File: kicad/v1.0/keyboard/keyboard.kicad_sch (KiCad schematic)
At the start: 89 parts, among them J1 PMOD, J2 Conn_01x02, J3 Conn_01x02, SW1 @, SW10 I, SW11 J, SW12 K, SW13 L, SW14 M, SW15 N, SW16 O, SW17 P, SW18 Q, SW19 R, SW2 A, SW20 S, SW21 T, SW22 U, SW23 V, SW24 W, SW25 X, SW26 Y, SW27 Z, SW28 0, SW29 1, SW3 B, SW30 2, SW31 3, SW32 4, SW33 5, SW34 6, SW35 7, SW36 0, SW37 1, SW38 2, SW39 3, SW4 C, SW40 4, SW41 5, SW42 6, SW43 7, SW44 8, SW45 9, SW46 ., SW47 8, SW48 9, SW49 :, SW5 D, SW50 ;, SW51 ,, SW52 -, SW53 ., SW54 /, SW55 ENTER, SW56 ENTER, SW57 CLEAR, SW58 BREAK, SW59 UP, SW6 E, SW60 DOWN, SW61 LEFT, SW62 RIGHT, SW63 SPACE, SW64 RESET, SW65 RSHIFT, SW66 LSHIFT, SW67 SPACE, SW68 SPACE, SW69 ENTER, SW7 F, SW8 G, SW9 H, U1 74LS07, U2 74LS138, U3 74LS07, U4 74LS157

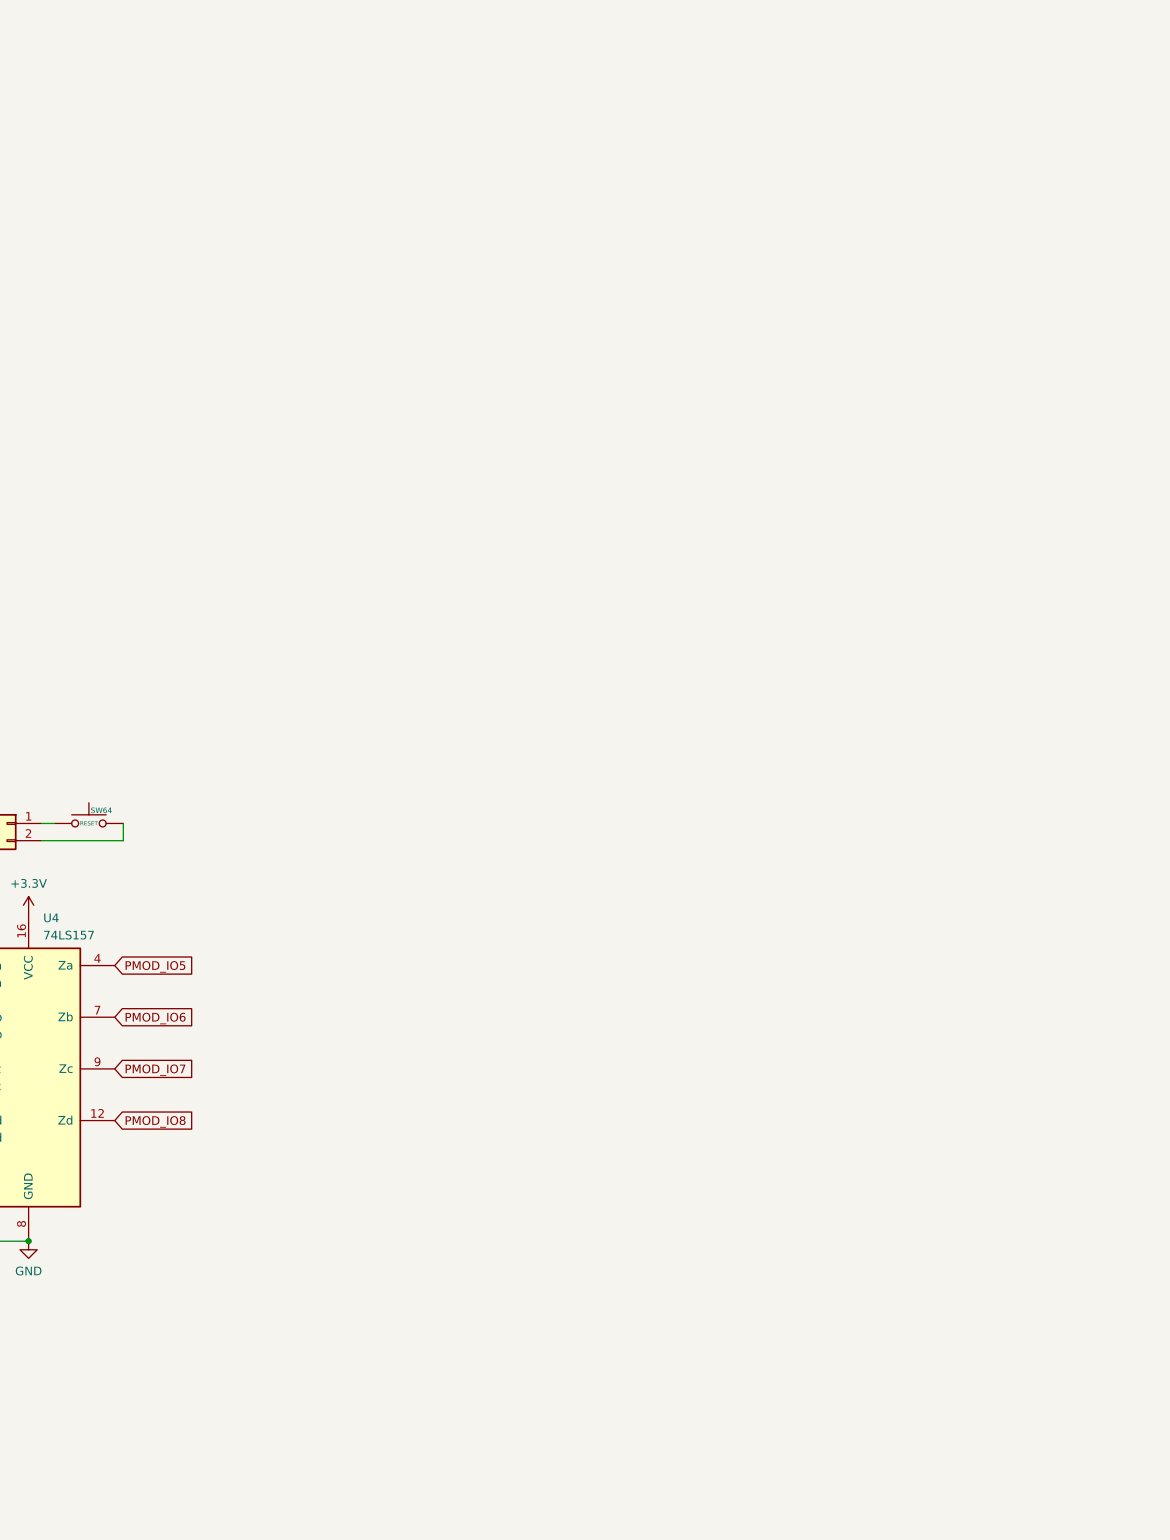
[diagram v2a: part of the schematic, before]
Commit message: Add schematics for interface PCB
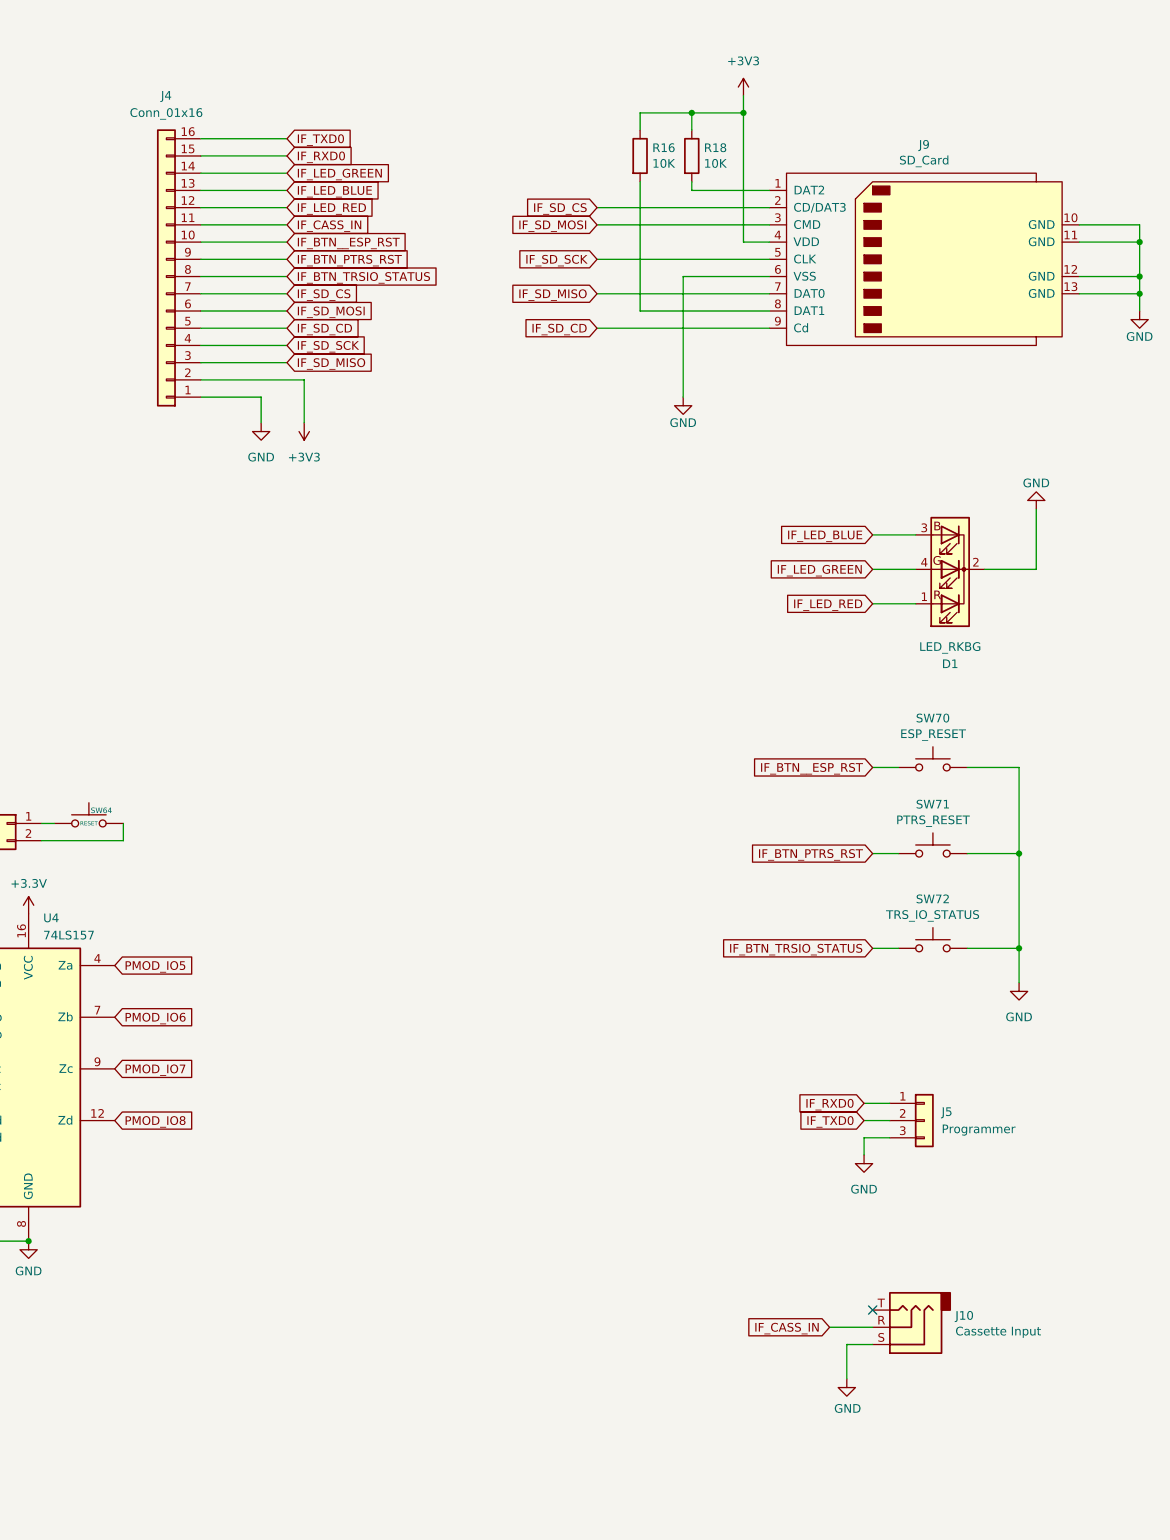
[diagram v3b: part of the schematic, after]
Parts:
- added D1: LED_RKBG, LED_THT:LED_D5.0mm-4_RGB, symbol Device:LED_RKBG
- added J10: Cassette Input, Library:Jack_3.5mm_CUI_SJ1-3535NG_Horizontal_CircularHoles, symbol Connector:AudioJack3
- added J4: Conn_01x16, Connector_PinHeader_2.54mm:PinHeader_1x16_P2.54mm_Vertical, symbol Connector_Generic:Conn_01x16
- added J5: Programmer, Connector_PinHeader_2.54mm:PinHeader_1x03_P2.54mm_Horizontal, symbol Connector_Generic:Conn_01x03
- added J9: SD_Card, Library:TFP09-2-12B, symbol SDCard:SD_Card
- added R16, R18: 10K, Resistor_SMD:R_0805_2012Metric_Pad1.20x1.40mm_HandSolder, symbol Device:R
- added SW70: ESP_RESET, Button_Switch_THT:SW_PUSH_6mm, symbol Switch:SW_Push
- added SW71: PTRS_RESET, Button_Switch_THT:SW_PUSH_6mm, symbol Switch:SW_Push
- added SW72: TRS_IO_STATUS, Button_Switch_THT:SW_PUSH_6mm, symbol Switch:SW_Push
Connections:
- net GND: now also D1.2 (K), J10.S, J4.1 (Pin_1), J5.3 (Pin_3), J9.10 (GND), J9.11 (GND), J9.12 (GND), J9.13 (GND), J9.6 (VSS), SW70.2, SW71.2, SW72.2
- new net: J9.1 (DAT2), R18.2
- new net: J9.8 (DAT1), R16.2
- new net +3V3: J4.2 (Pin_2), J9.4 (VDD), R16.1, R18.1
- new net IF_BTN_PTRS_RST: J4.9 (Pin_9), SW71.1
- new net IF_BTN_TRSIO_STATUS: J4.8 (Pin_8), SW72.1
- new net IF_BTN__ESP_RST: J4.10 (Pin_10), SW70.1
- new net IF_CASS_IN: J10.R, J4.11 (Pin_11)
- new net IF_LED_BLUE: D1.3 (BA), J4.13 (Pin_13)
- new net IF_LED_GREEN: D1.4 (GA), J4.14 (Pin_14)
- new net IF_LED_RED: D1.1 (RA), J4.12 (Pin_12)
- new net IF_RXD0: J4.15 (Pin_15), J5.1 (Pin_1)
- new net IF_SD_CD: J4.5 (Pin_5), J9.9 (Cd)
- new net IF_SD_CS: J4.7 (Pin_7), J9.2 (CD/DAT3)
- new net IF_SD_MISO: J4.3 (Pin_3), J9.7 (DAT0)
- new net IF_SD_MOSI: J4.6 (Pin_6), J9.3 (CMD)
- new net IF_SD_SCK: J4.4 (Pin_4), J9.5 (CLK)
- new net IF_TXD0: J4.16 (Pin_16), J5.2 (Pin_2)
- no-connect marks 4 -> 5

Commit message: Updated Interface board
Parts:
- removed J10: Cassette Input, Library:Jack_3.5mm_CUI_SJ1-3535NG_Horizontal_CircularHoles, symbol Connector:AudioJack3
- removed J4: Conn_01x16, Connector_PinHeader_2.54mm:PinHeader_1x16_P2.54mm_Vertical, symbol Connector_Generic:Conn_01x16
- added J10: Cassette Input, Connector_Audio:Jack_3.5mm_CUI_SJ1-3525N_Horizontal, symbol Connector_Audio:AudioJack3_SwitchTR
- added J11: Cassette Output, Connector_Audio:Jack_3.5mm_CUI_SJ1-3525N_Horizontal, symbol Connector_Audio:AudioJack3_SwitchTR
- added J12: SD_Card, Library:TFP09-2-12B, symbol SDCard:SD_Card
- added J4: Interface Connector, Connector_PinHeader_1.27mm:PinHeader_2x10_P1.27mm_Vertical, symbol Connector_Generic:Conn_02x10_Odd_Even
- SW70, SW71, SW72: footprint Button_Switch_THT:SW_PUSH_6mm -> Button_Switch_THT:SW_Tactile_SPST_Angled_PTS645Vx83-2LFS
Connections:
- net +3V3: now also J12.4 (VDD), J4.19 (Pin_19), J4.20 (Pin_20)
- net GND: now also J10.S, J11.S, J12.10 (GND), J12.11 (GND), J12.12 (GND), J12.13 (GND), J12.6 (VSS), J4.17 (Pin_17), J4.18 (Pin_18), J4.2 (Pin_2)
- net IF_BTN_PTRS_RST: now also J4.10 (Pin_10)
- net IF_BTN_TRSIO_STATUS: now also J4.12 (Pin_12)
- net IF_BTN__ESP_RST: now also J4.9 (Pin_9)
- net IF_CASS_IN: now also J10.T, J4.8 (Pin_8)
- net IF_LED_BLUE: now also J4.5 (Pin_5)
- net IF_LED_GREEN: now also J4.7 (Pin_7)
- net IF_LED_RED: now also J4.3 (Pin_3)
- net IF_RXD0: now also J4.6 (Pin_6)
- net IF_SD_CD: now also J12.9 (Cd), J4.15 (Pin_15)
- net IF_SD_CS: now also J12.2 (CD/DAT3), J4.14 (Pin_14)
- net IF_SD_MISO: now also J12.7 (DAT0), J4.11 (Pin_11)
- net IF_SD_MOSI: now also J12.3 (CMD), J4.16 (Pin_16)
- net IF_SD_SCK: now also J12.5 (CLK), J4.13 (Pin_13)
- net IF_TXD0: now also J4.4 (Pin_4)
- net at J9.1 (DAT2), R18.2: now also J12.1 (DAT2)
- net at J9.8 (DAT1), R16.2: now also J12.8 (DAT1)
- new net IF_CASS_OUT: J11.T, J4.1 (Pin_1)
- no-connect marks 5 -> 10
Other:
- moved on the sheet: D1, SW70, SW71, SW72

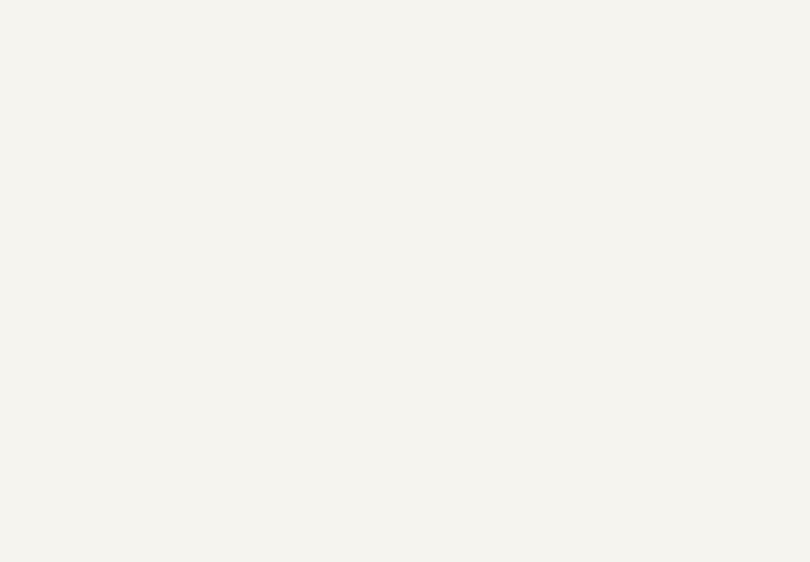
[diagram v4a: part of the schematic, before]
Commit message: Interface board with Barrel Jack for power
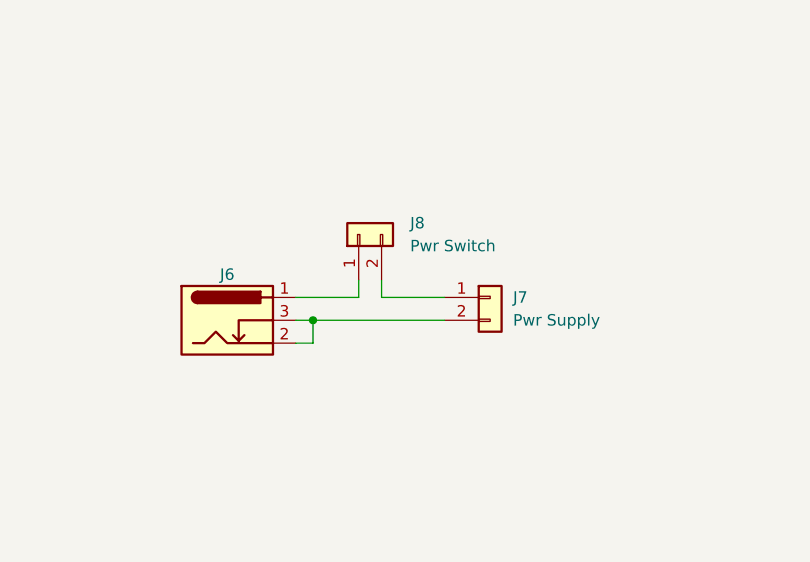
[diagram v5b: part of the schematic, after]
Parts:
- added J6: Barrel_Jack_Switch, Connector_BarrelJack:BarrelJack_Horizontal, symbol Connector:Barrel_Jack_Switch
- added J7: Pwr Supply, Connector_PinHeader_2.54mm:PinHeader_1x02_P2.54mm_Vertical, symbol Connector_Generic:Conn_01x02
- added J8: Pwr Switch, Connector_PinHeader_2.54mm:PinHeader_1x02_P2.54mm_Vertical, symbol Connector_Generic:Conn_01x02
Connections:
- new net: J6.1, J8.1 (Pin_1)
- new net: J7.1 (Pin_1), J8.2 (Pin_2)
- new net: J6.2, J6.3, J7.2 (Pin_2)
